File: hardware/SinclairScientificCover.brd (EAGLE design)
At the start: 48.3 x 109.2 mm, 23 parts

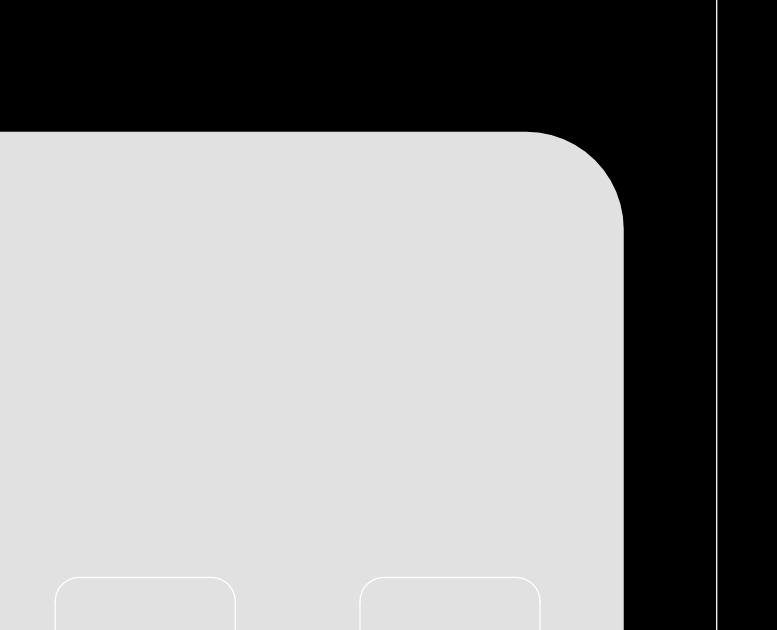
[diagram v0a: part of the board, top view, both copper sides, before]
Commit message: Changed on/off switch to SMD type, fixed some DFM issues
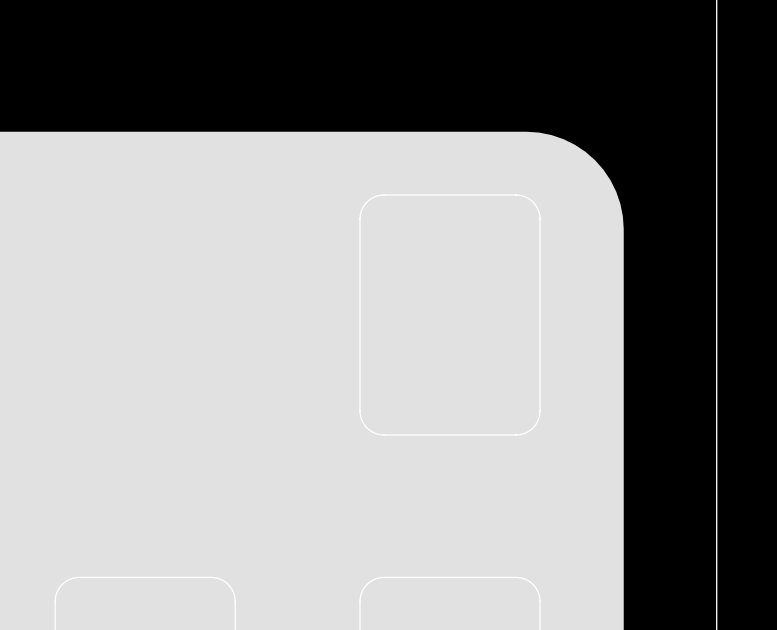
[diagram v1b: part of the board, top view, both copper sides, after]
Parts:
- added E$20: (no value), SinclairScientific:HOLE-PWR
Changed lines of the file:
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@@
 <setting verticaltext="up"/>
 </settings>
-<grid distance="12.5" unitdist="mil" unit="mil" style="dots" multiple="2" display="yes" altdistance="1" altunitdist="mil" altunit="mil"/>
+<grid distance="12.5" unitdist="mil" unit="mil" style="dots" multiple="2" display="yes" altdistance="6.25" altunitdist="mil" altunit="mil"/>
 <layers>
 <layer number="1" name="Top" color="4" fill="1" visible="yes" active="yes"/>
@@
 <layer number="19" name="Unrouted" color="6" fill="1" visible="yes" active="yes"/>
 <layer number="20" name="Dimension" color="15" fill="1" visible="yes" active="yes"/>
-<layer number="21" name="tPlace" color="14" fill="1" visible="yes" active="yes"/>
+<layer number="21" name="tPlace" color="14" fill="1" visible="no" active="yes"/>
 <layer number="22" name="bPlace" color="13" fill="1" visible="yes" active="yes"/>
 <layer number="23" name="tOrigins" color="14" fill="1" visible="yes" active="yes"/>
@@
 </class>
 </classes>
-<designrules name="pcbway-2layer-12mm">
+<designrules name="default *">
 <description language="de">&lt;b&gt;EAGLE Design Rules&lt;/b&gt;
 &lt;p&gt;
@@
 <param name="layerSetup" value="(1*16)"/>
 <param name="mtCopper" value="0.035mm 0.035mm 0.035mm 0.035mm 0.035mm 0.035mm 0.035mm 0.035mm 0.035mm 0.035mm 0.035mm 0.035mm 0.035mm 0.035mm 0.035mm 0.035mm"/>
-<param name="mtIsolate" value="1.13mm 0.73mm 0.2mm 0.15mm 0.2mm 0.15mm 0.2mm 0.15mm 0.2mm 0.15mm 0.2mm 0.15mm 0.2mm 0.15mm 0.11mm"/>
+<param name="mtIsolate" value="1.93mm 0.73mm 0.2mm 0.15mm 0.2mm 0.15mm 0.2mm 0.15mm 0.2mm 0.15mm 0.2mm 0.15mm 0.2mm 0.15mm 0.11mm"/>
 <param name="mdWireWire" value="7mil"/>
 <param name="mdWirePad" value="7mil"/>
@@
 <element name="U$26" library="SinclairScientific" package="HOLE_3-48" value="" x="44.45" y="2.54"/>
 <element name="U$27" library="SinclairScientific" package="HOLE_3-48" value="" x="2.54" y="2.54"/>
-<element name="E$1" library="SinclairScientific" package="HOLE-1S_CAP" value="" x="8.255" y="12.065"/>
-<element name="E$2" library="SinclairScientific" package="HOLE-1S_CAP" value="" x="18.415" y="12.065"/>
-<element name="E$3" library="SinclairScientific" package="HOLE-1S_CAP" value="" x="28.575" y="12.065"/>
-<element name="E$4" library="SinclairScientific" package="HOLE-1S_CAP" value="" x="38.735" y="12.065"/>
-<element name="E$5" library="SinclairScientific" package="HOLE-1S_CAP" value="" x="38.735" y="22.86"/>
-<element name="E$6" library="SinclairScientific" package="HOLE-1S_CAP" value="" x="28.575" y="22.86"/>
-<element name="E$7" library="SinclairScientific" package="HOLE-1S_CAP" value="" x="18.415" y="22.86"/>
-<element name="E$8" library="SinclairScientific" package="HOLE-1S_CAP" value="" x="8.255" y="22.86"/>
-<element name="E$9" library="SinclairScientific" package="HOLE-1S_CAP" value="" x="8.255" y="33.655"/>
-<element name="E$10" library="SinclairScientific" package="HOLE-1S_CAP" value="" x="18.415" y="33.655"/>
-<element name="E$11" library="SinclairScientific" package="HOLE-1S_CAP" value="" x="28.575" y="33.655"/>
-<element name="E$12" library="SinclairScientific" package="HOLE-1S_CAP" value="" x="38.735" y="33.655"/>
-<element name="E$13" library="SinclairScientific" package="HOLE-1S_CAP" value="" x="38.735" y="44.45"/>
-<element name="E$14" library="SinclairScientific" package="HOLE-1S_CAP" value="" x="28.575" y="44.45"/>
-<element name="E$15" library="SinclairScientific" package="HOLE-1S_CAP" value="" x="18.415" y="44.45"/>
-<element name="E$16" library="SinclairScientific" package="HOLE-1S_CAP" value="" x="8.255" y="44.45"/>
-<element name="E$17" library="SinclairScientific" package="HOLE-1S_CAP" value="" x="8.255" y="55.245"/>
-<element name="E$18" library="SinclairScientific" package="HOLE-1S_CAP" value="" x="18.415" y="55.245"/>
+<element name="E$1" library="SinclairScientific" library_urn="urn:adsk.eagle:library:6524367" package="HOLE-1S_CAP" package3d_urn="urn:adsk.eagle:package:6524816/1" value="" x="8.255" y="12.065"/>
+<element name="E$2" library="SinclairScientific" library_urn="urn:adsk.eagle:library:6524367" package="HOLE-1S_CAP" package3d_urn="urn:adsk.eagle:package:6524816/1" value="" x="18.415" y="12.065"/>
+<element name="E$3" library="SinclairScientific" library_urn="urn:adsk.eagle:library:6524367" package="HOLE-1S_CAP" package3d_urn="urn:adsk.eagle:package:6524816/1" value="" x="28.575" y="12.065"/>
+<element name="E$4" library="SinclairScientific" library_urn="urn:adsk.eagle:library:6524367" package="HOLE-1S_CAP" package3d_urn="urn:adsk.eagle:package:6524816/1" value="" x="38.735" y="12.065"/>
+<element name="E$5" library="SinclairScientific" library_urn="urn:adsk.eagle:library:6524367" package="HOLE-1S_CAP" package3d_urn="urn:adsk.eagle:package:6524816/1" value="" x="38.735" y="22.86"/>
+<element name="E$6" library="SinclairScientific" library_urn="urn:adsk.eagle:library:6524367" package="HOLE-1S_CAP" package3d_urn="urn:adsk.eagle:package:6524816/1" value="" x="28.575" y="22.86"/>
+<element name="E$7" library="SinclairScientific" library_urn="urn:adsk.eagle:library:6524367" package="HOLE-1S_CAP" package3d_urn="urn:adsk.eagle:package:6524816/1" value="" x="18.415" y="22.86"/>
+<element name="E$8" library="SinclairScientific" library_urn="urn:adsk.eagle:library:6524367" package="HOLE-1S_CAP" package3d_urn="urn:adsk.eagle:package:6524816/1" value="" x="8.255" y="22.86"/>
+<element name="E$9" library="SinclairScientific" library_urn="urn:adsk.eagle:library:6524367" package="HOLE-1S_CAP" package3d_urn="urn:adsk.eagle:package:6524816/1" value="" x="8.255" y="33.655"/>
+<element name="E$10" library="SinclairScientific" library_urn="urn:adsk.eagle:library:6524367" package="HOLE-1S_CAP" package3d_urn="urn:adsk.eagle:package:6524816/1" value="" x="18.415" y="33.655"/>
+<element name="E$11" library="SinclairScientific" library_urn="urn:adsk.eagle:library:6524367" package="HOLE-1S_CAP" package3d_urn="urn:adsk.eagle:package:6524816/1" value="" x="28.575" y="33.655"/>
+<element name="E$12" library="SinclairScientific" library_urn="urn:adsk.eagle:library:6524367" package="HOLE-1S_CAP" package3d_urn="urn:adsk.eagle:package:6524816/1" value="" x="38.735" y="33.655"/>
+<element name="E$13" library="SinclairScientific" library_urn="urn:adsk.eagle:library:6524367" package="HOLE-1S_CAP" package3d_urn="urn:adsk.eagle:package:6524816/1" value="" x="38.735" y="44.45"/>
+<element name="E$14" library="SinclairScientific" library_urn="urn:adsk.eagle:library:6524367" package="HOLE-1S_CAP" package3d_urn="urn:adsk.eagle:package:6524816/1" value="" x="28.575" y="44.45"/>
+<element name="E$15" library="SinclairScientific" library_urn="urn:adsk.eagle:library:6524367" package="HOLE-1S_CAP" package3d_urn="urn:adsk.eagle:package:6524816/1" value="" x="18.415" y="44.45"/>
+<element name="E$16" library="SinclairScientific" library_urn="urn:adsk.eagle:library:6524367" package="HOLE-1S_CAP" package3d_urn="urn:adsk.eagle:package:6524816/1" value="" x="8.255" y="44.45"/>
+<element name="E$17" library="SinclairScientific" library_urn="urn:adsk.eagle:library:6524367" package="HOLE-1S_CAP" package3d_urn="urn:adsk.eagle:package:6524816/1" value="" x="8.255" y="55.245"/>
+<element name="E$18" library="SinclairScientific" library_urn="urn:adsk.eagle:library:6524367" package="HOLE-1S_CAP" package3d_urn="urn:adsk.eagle:package:6524816/1" value="" x="18.415" y="55.245"/>
 <element name="E$19" library="SinclairScientific" package="SILK_EVERYTHING" value="" x="23.495" y="59.055"/>
+<element name="E$20" library="SinclairScientific" library_urn="urn:adsk.eagle:library:6524367" package="HOLE-PWR" value="" x="38.735" y="56.1975"/>
 </elements>
 <signals>
@@
 <mfgpreviewcolor name="substratecolor" color="0xFF786E46"/>
 </mfgpreviewcolors>
-<errors>
-</errors>
 </board>
 </drawing>
+<compatibility>
+<note version="8.2" severity="warning">
+Since Version 8.2, EAGLE supports online libraries. The ids
+of those online libraries will not be understood (or retained)
+with this version.
+</note>
+<note version="8.3" severity="warning">
+Since Version 8.3, EAGLE supports URNs for individual library
+assets (packages, symbols, and devices). The URNs of those assets
+will not be understood (or retained) with this version.
+</note>
+<note version="8.3" severity="warning">
+Since Version 8.3, EAGLE supports the association of 3D packages
+with devices in libraries, schematics, and board files. Those 3D
+packages will not be understood (or retained) with this version.
+</note>
+</compatibility>
 </eagle>

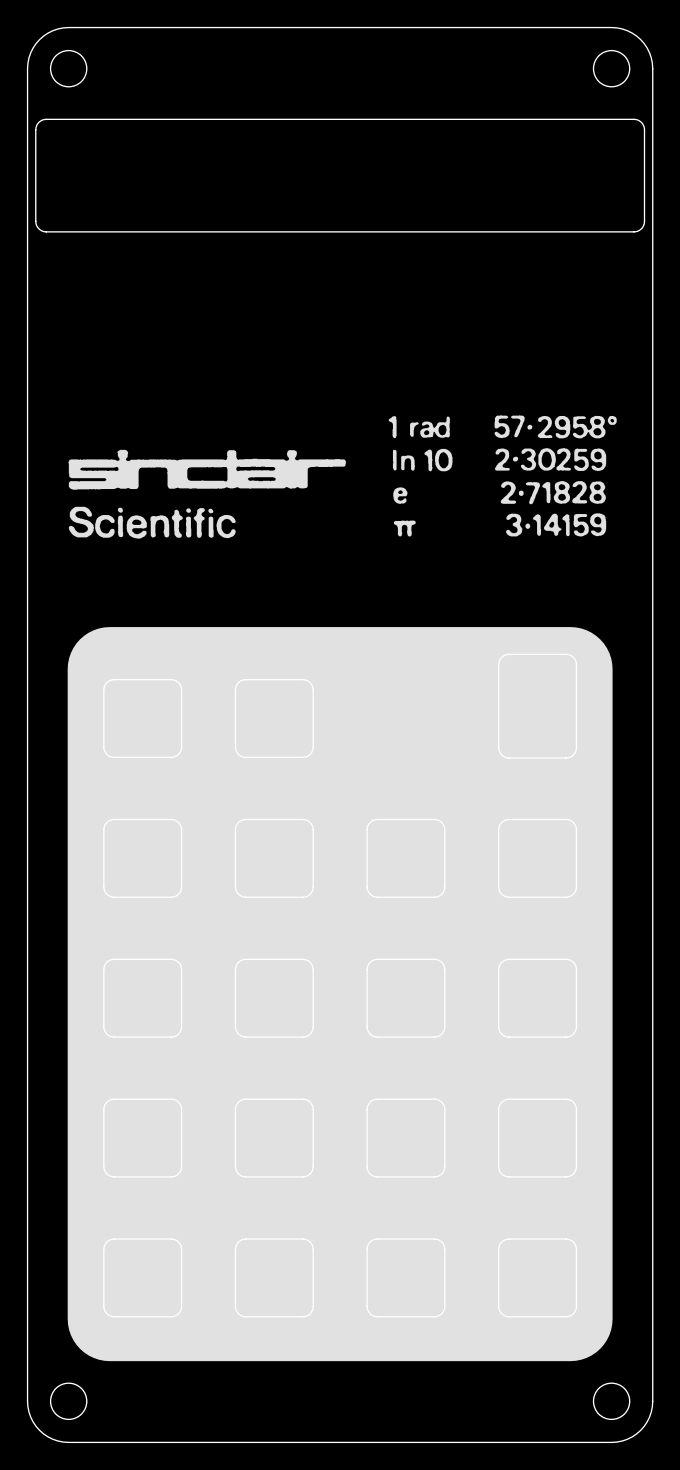
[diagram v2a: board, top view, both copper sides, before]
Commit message: Finalized top layer of faceplate board
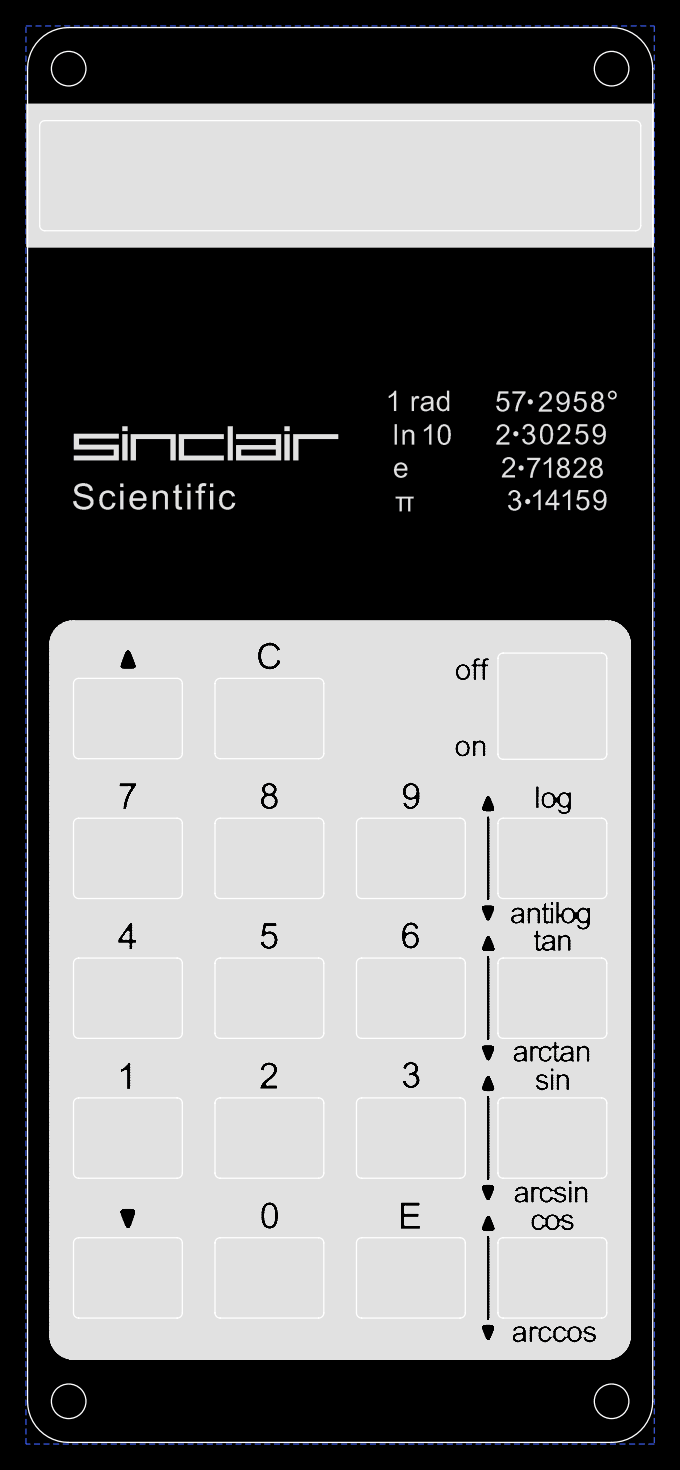
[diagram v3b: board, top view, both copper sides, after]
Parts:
- added E$21: (no value), SinclairScientific:SILK_BTN_UP
- added E$22: (no value), SinclairScientific:SILK_BTN_7
- added E$23: (no value), SinclairScientific:SILK_BTN_8
- added E$24: (no value), SinclairScientific:SILK_BTN_9
- added E$25: (no value), SinclairScientific:SILK_BTN_4
- added E$26: (no value), SinclairScientific:SILK_BTN_5
- added E$27: (no value), SinclairScientific:SILK_BTN_6
- added E$28: (no value), SinclairScientific:SILK_BTN_3
- added E$29: (no value), SinclairScientific:SILK_BTN_2
- added E$30: (no value), SinclairScientific:SILK_BTN_1
- added E$31: (no value), SinclairScientific:SILK_BTN_0
- added E$32: (no value), SinclairScientific:SILK_BTN_DOWN
- added E$33: (no value), SinclairScientific:SILK_BTN_E
- added E$34: (no value), SinclairScientific:SILK_BTN_COS
- added E$35: (no value), SinclairScientific:SILK_BTN_ARCCOS
- added E$36: (no value), SinclairScientific:SILK_BTN_ARCSIN
- added E$37: (no value), SinclairScientific:SILK_BTN_SIN
- added E$38: (no value), SinclairScientific:SILK_BTN_ARCTAN
- added E$39: (no value), SinclairScientific:SILK_BTN_TAN
- added E$40: (no value), SinclairScientific:SILK_BTN_ANTILOG
- added E$41: (no value), SinclairScientific:SILK_BTN_LOG
- added E$42: (no value), SinclairScientific:SILK_BTN_ON
- added E$43: (no value), SinclairScientific:SILK_BTN_OFF
- added E$44, E$45, E$46, E$47: (no value), SinclairScientific:SILK_BTN_FUNC_ARROWS
- added E$48: (no value), SinclairScientific:LOGO_PLH_1750
- added E$49: (no value), SinclairScientific:SILK_REF_TEXT
- added E$50: (no value), SinclairScientific:SILK_SINCLAIR_LOGO
- E$19: device SinclairScientific:SILK_EVERYTHING -> SinclairScientific:SILK_BTN_C
- U$14, U$23, U$26, U$27: device SinclairScientific:HOLE_3-48 -> SinclairScientific:HOLE_3-48_NO-STOP
- moved E$19 5.56 mm to (18.0, 60.1)
- moved E$1 1.14 mm to (7.11, 12.1)
- moved E$12 1.14 mm to (39.9, 33.7)
- moved E$13 1.14 mm to (39.9, 44.5)
- moved E$16 1.14 mm to (7.11, 44.5)
- moved E$17 1.14 mm to (7.11, 55.2)
- moved E$20 1.14 mm to (39.9, 56.2)
- moved E$4 1.14 mm to (39.9, 12.1)
- moved E$5 1.14 mm to (39.9, 22.9)
- moved E$8 1.14 mm to (7.11, 22.9)
- moved E$9 1.14 mm to (7.11, 33.7)
- moved E$10 0.38 mm to (18.0, 33.7)
- moved E$11 0.38 mm to (29.0, 33.7)
- moved E$14 0.38 mm to (29.0, 44.5)
- moved E$15 0.38 mm to (18.0, 44.5)
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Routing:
- added copper zone on layer 16, net COPPER
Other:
- outline, holes or cut-outs redrawn

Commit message: Increased coverplate silkscreen text width
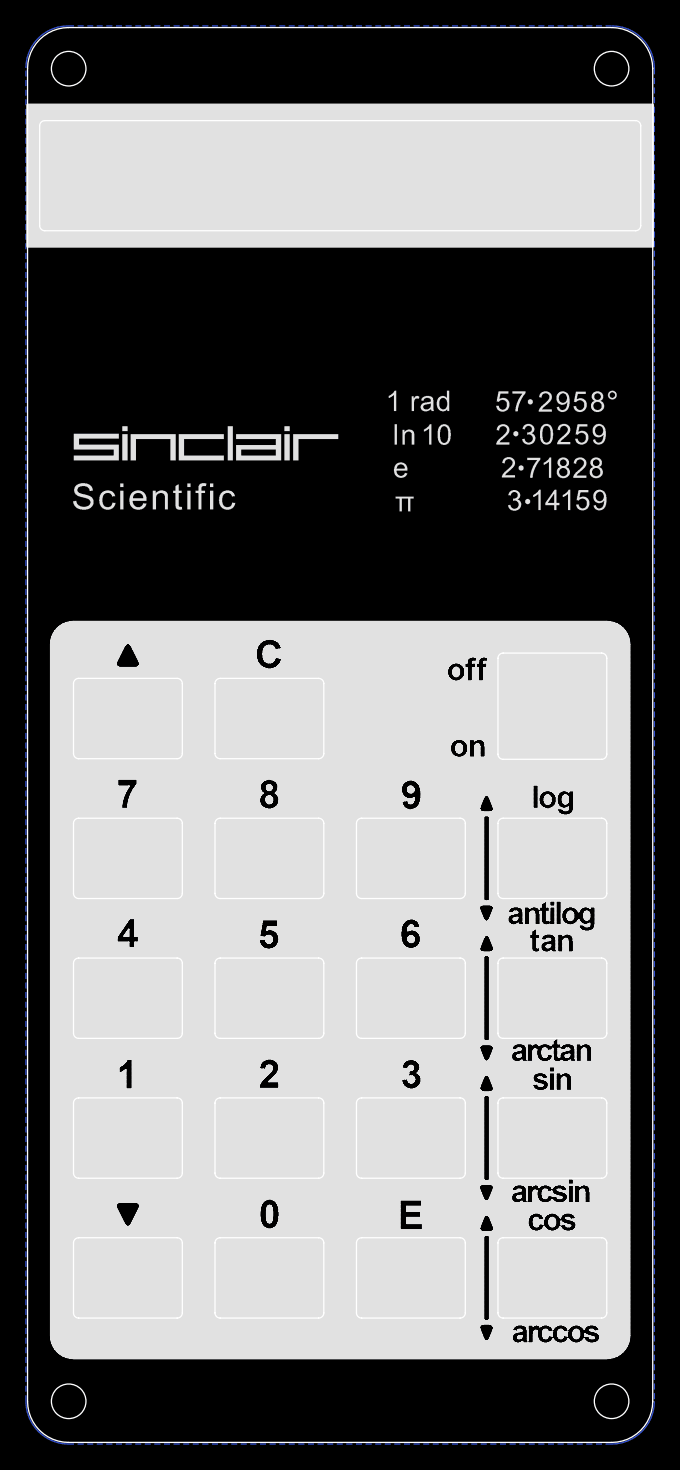
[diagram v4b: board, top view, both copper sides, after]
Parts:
- removed E$32: (no value), SinclairScientific:SILK_BTN_DOWN
- added E$51: (no value), SinclairScientific:SILK_SIGNATURES
- added E$52: (no value), SinclairScientific:SILK_BTN_UP
- moved E$21 0.38 mm to (7.11, 60.1)
- moved E$43 0.38 mm to (33.4, 58.9)
- moved E$42 0.25 mm to (33.4, 53.0)
- moved E$26 0.13 mm to (18.0, 38.7)
- moved E$27 0.13 mm to (29.0, 38.7)
- moved E$28 0.13 mm to (29.0, 27.9)
- moved E$30 0.13 mm to (7.11, 27.7)
- moved E$31 0.13 mm to (18.0, 17.0)
- moved E$33 0.13 mm to (29.0, 17.0)
- moved E$29 0.13 mm to (18.0, 27.8)
- moved E$19 0.13 mm to (18.0, 60.2)
- moved E$22 0.13 mm to (7.14, 49.5)
- moved E$23 0.13 mm to (18.0, 49.5)
- moved E$24 0.13 mm to (29.0, 49.6)
- moved E$25 0.13 mm to (7.09, 38.5)
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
